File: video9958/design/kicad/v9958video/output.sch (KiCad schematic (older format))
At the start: 28 parts, among them J2 Conn_02x06_Counter_Clockwise, J3 DIN-6, Q2 2N3904, Q3 2N3906, Q4 2N3906, Q5 2N3906

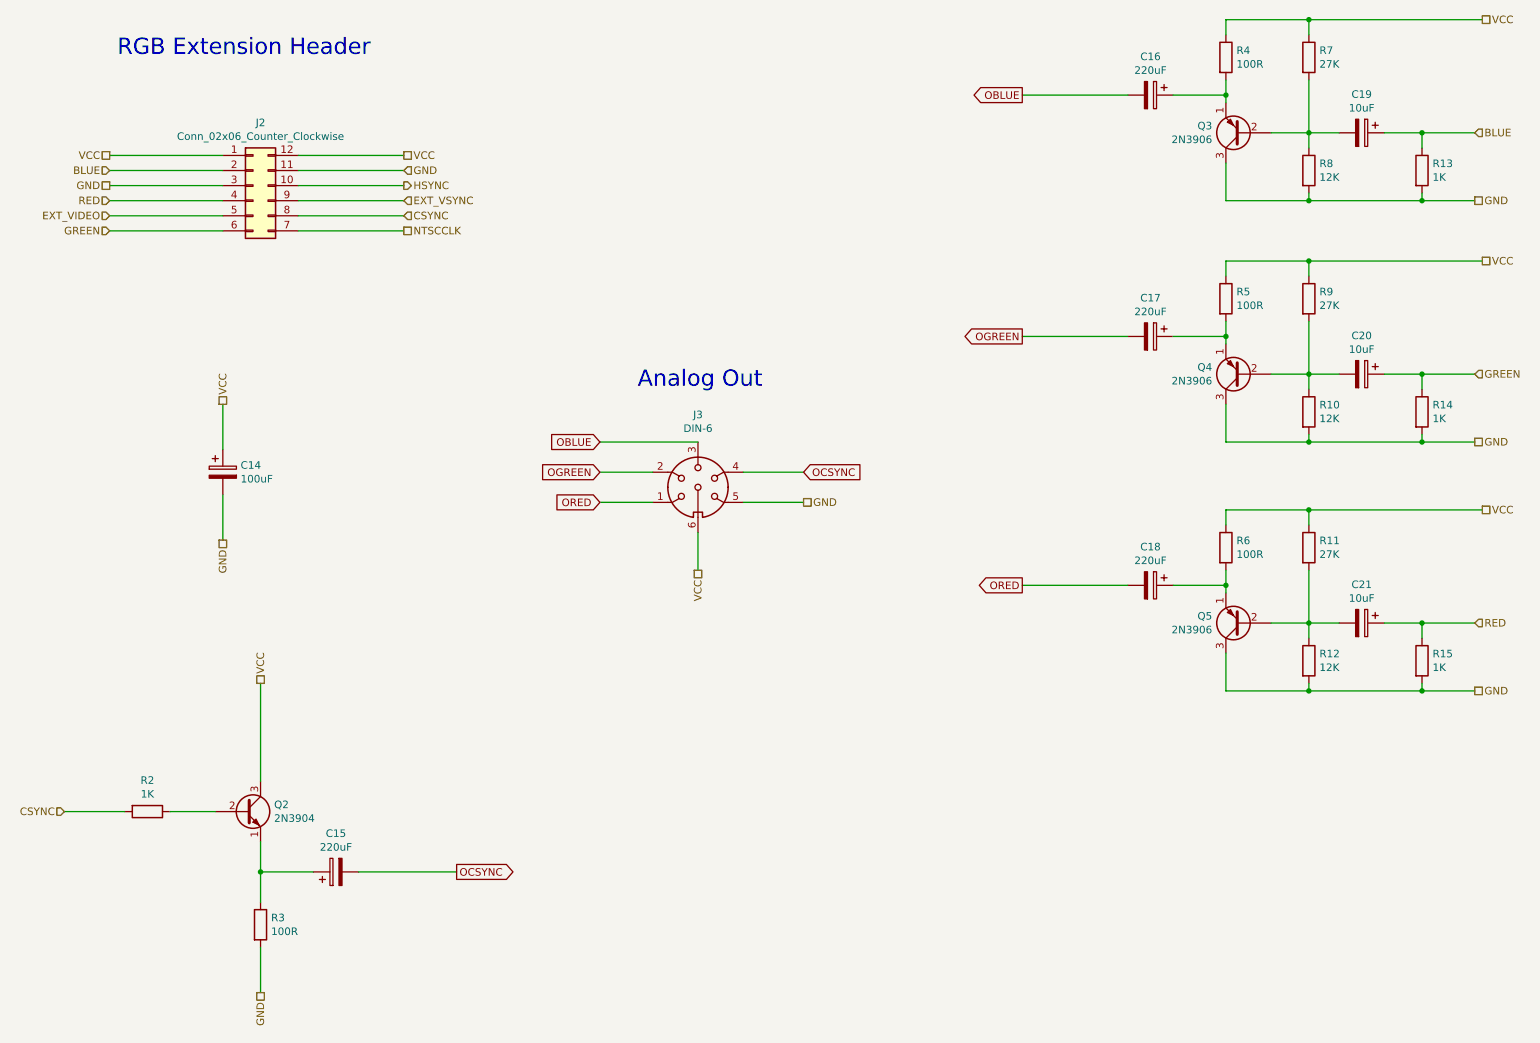
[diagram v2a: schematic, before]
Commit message: Rev 1 - Four layer board
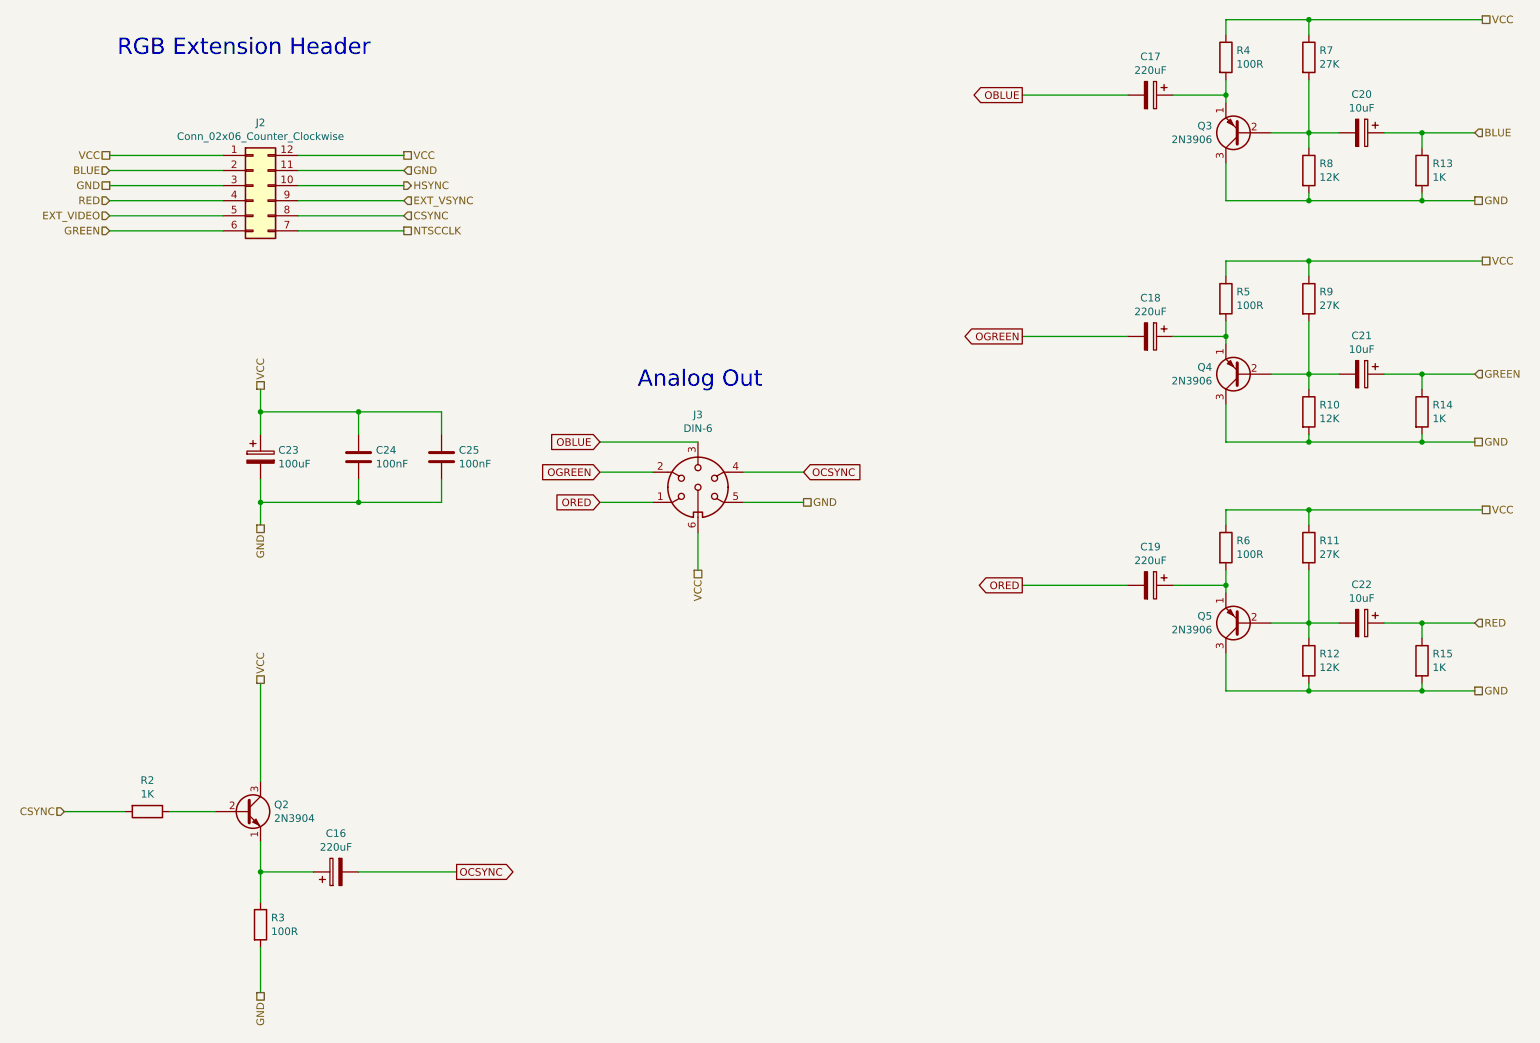
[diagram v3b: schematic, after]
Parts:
- added C24, C25: 100nF, Capacitor_THT:C_Rect_L7.0mm_W2.5mm_P5.00mm, symbol Device:C
- renumbered C15 to C16, C16 to C17, C17 to C18, C18 to C19, C19 to C20, C20 to C21, C21 to C22, C14 to C23
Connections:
- net GND: now also C24.2, C25.2
- net VCC: now also C24.1, C25.1
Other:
- moved on the sheet: C23
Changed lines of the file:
@@
 	2800 6450 2450 6450
 $Comp
-L Device:CP C15
+L Device:CP C16
 U 1 1 5EB8D33A
 P 2950 6450
-F 0 "C15" V 3205 6450 50  0000 C CNN
+F 0 "C16" V 3205 6450 50  0000 C CNN
 F 1 "220uF" V 3114 6450 50  0000 C CNN
 F 2 "Capacitor_THT:CP_Radial_D6.3mm_P2.50mm" H 2988 6300 50  0001 C CNN
@@
 $EndComp
 $Comp
-L Device:CP C21
+L Device:CP C22
 U 1 1 5EB704B0
 P 9750 4800
-F 0 "C21" V 9495 4800 50  0000 C CNN
+F 0 "C22" V 9495 4800 50  0000 C CNN
 F 1 "10uF" V 9586 4800 50  0000 C CNN
 F 2 "Capacitor_THT:CP_Radial_D5.0mm_P2.50mm" H 9788 4650 50  0001 C CNN
@@
 	8850 2800 8850 2900
 $Comp
-L Device:CP C17
+L Device:CP C18
 U 1 1 5EB5A4E3
 P 8350 2900
-F 0 "C17" V 8095 2900 50  0000 C CNN
+F 0 "C18" V 8095 2900 50  0000 C CNN
 F 1 "220uF" V 8186 2900 50  0000 C CNN
 F 2 "Capacitor_THT:CP_Radial_D6.3mm_P2.50mm" H 8388 2750 50  0001 C CNN
@@
 $EndComp
 $Comp
-L Device:CP C20
+L Device:CP C21
 U 1 1 5EB5A4AC
 P 9750 3150
-F 0 "C20" V 9495 3150 50  0000 C CNN
+F 0 "C21" V 9495 3150 50  0000 C CNN
 F 1 "10uF" V 9586 3150 50  0000 C CNN
 F 2 "Capacitor_THT:CP_Radial_D5.0mm_P2.50mm" H 9788 3000 50  0001 C CNN
@@
 	8850 1200 8850 1300
 $Comp
-L Device:CP C16
+L Device:CP C17
 U 1 1 5EB51CD3
 P 8350 1300
-F 0 "C16" V 8095 1300 50  0000 C CNN
+F 0 "C17" V 8095 1300 50  0000 C CNN
 F 1 "220uF" V 8186 1300 50  0000 C CNN
 F 2 "Capacitor_THT:CP_Radial_D6.3mm_P2.50mm" H 8388 1150 50  0001 C CNN
@@
 $EndComp
 $Comp
-L Device:CP C19
+L Device:CP C20
 U 1 1 5EB4735D
 P 9750 1550
-F 0 "C19" V 9495 1550 50  0000 C CNN
+F 0 "C20" V 9495 1550 50  0000 C CNN
 F 1 "10uF" V 9586 1550 50  0000 C CNN
 F 2 "Capacitor_THT:CP_Radial_D5.0mm_P2.50mm" H 9788 1400 50  0001 C CNN
@@
 	2700 1700 3400 1700
 $Comp
-L Device:CP C14
+L Device:CP C23
 U 1 1 5ECAC019
-P 2200 3800
-F 0 "C14" H 2318 3846 50  0000 L CNN
-F 1 "100uF" H 2318 3755 50  0000 L CNN
-F 2 "Capacitor_THT:CP_Radial_D5.0mm_P2.50mm" H 2238 3650 50  0001 C CNN
-F 3 "~" H 2200 3800 50  0001 C CNN
-	1    2200 3800
-	1    0    0    -1
-$EndComp
-Wire Wire Line
-	2200 3350 2200 3650
-Wire Wire Line
-	2200 3950 2200 4250
-Text HLabel 2200 3350 1    50   UnSpc ~ 0
-VCC
-Text HLabel 2200 4250 3    50   UnSpc ~ 0
-GND
-$Comp
-L Device:CP C18
+P 2450 3700
+F 0 "C23" H 2568 3746 50  0000 L CNN
+F 1 "100uF" H 2568 3655 50  0000 L CNN
+F 2 "Capacitor_THT:CP_Radial_D5.0mm_P2.50mm" H 2488 3550 50  0001 C CNN
+F 3 "~" H 2450 3700 50  0001 C CNN
+	1    2450 3700
+	1    0    0    -1
+$EndComp
+Wire Wire Line
+	2450 3250 2450 3400
+Wire Wire Line
+	2450 3850 2450 4000
+Text HLabel 2450 3250 1    50   UnSpc ~ 0
+VCC
+Text HLabel 2450 4150 3    50   UnSpc ~ 0
+GND
+$Comp
+L Device:CP C19
 U 1 1 5EB704E7
 P 8350 4550
-F 0 "C18" V 8095 4550 50  0000 C CNN
+F 0 "C19" V 8095 4550 50  0000 C CNN
 F 1 "220uF" V 8186 4550 50  0000 C CNN
 F 2 "Capacitor_THT:CP_Radial_D6.3mm_P2.50mm" H 8388 4400 50  0001 C CNN
@@
 	0    1    1    0
 $EndComp
+$Comp
+L Device:C C24
+U 1 1 5ECC1F41
+P 3100 3700
+F 0 "C24" H 3215 3746 50  0000 L CNN
+F 1 "100nF" H 3215 3655 50  0000 L CNN
+F 2 "Capacitor_THT:C_Rect_L7.0mm_W2.5mm_P5.00mm" H 3138 3550 50  0001 C CNN
+F 3 "~" H 3100 3700 50  0001 C CNN
+	1    3100 3700
+	1    0    0    -1
+$EndComp
+$Comp
+L Device:C C25
+U 1 1 5ECC26DA
+P 3650 3700
+F 0 "C25" H 3765 3746 50  0000 L CNN
+F 1 "100nF" H 3765 3655 50  0000 L CNN
+F 2 "Capacitor_THT:C_Rect_L7.0mm_W2.5mm_P5.00mm" H 3688 3550 50  0001 C CNN
+F 3 "~" H 3650 3700 50  0001 C CNN
+	1    3650 3700
+	1    0    0    -1
+$EndComp
+Wire Wire Line
+	3100 3550 3100 3400
+Wire Wire Line
+	3100 3400 2450 3400
+Connection ~ 2450 3400
+Wire Wire Line
+	2450 3400 2450 3550
+Wire Wire Line
+	3100 3400 3650 3400
+Wire Wire Line
+	3650 3400 3650 3550
+Connection ~ 3100 3400
+Wire Wire Line
+	3650 3850 3650 4000
+Wire Wire Line
+	3650 4000 3100 4000
+Connection ~ 2450 4000
+Wire Wire Line
+	2450 4000 2450 4150
+Wire Wire Line
+	3100 3850 3100 4000
+Connection ~ 3100 4000
+Wire Wire Line
+	3100 4000 2450 4000
 $EndSCHEMATC

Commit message: Revision 1.1 RTM
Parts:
- added C26: 100nF, Capacitor_THT:C_Rect_L7.0mm_W2.5mm_P5.00mm, symbol Device:C
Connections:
- net GND: now also C26.2
- net VCC: now also C26.1
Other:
- moved on the sheet: C23, C24, C25
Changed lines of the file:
@@
 L Device:CP C23
 U 1 1 5ECAC019
-P 2450 3700
-F 0 "C23" H 2568 3746 50  0000 L CNN
-F 1 "100uF" H 2568 3655 50  0000 L CNN
-F 2 "Capacitor_THT:CP_Radial_D5.0mm_P2.50mm" H 2488 3550 50  0001 C CNN
-F 3 "~" H 2450 3700 50  0001 C CNN
-	1    2450 3700
+P 1600 3700
+F 0 "C23" H 1718 3746 50  0000 L CNN
+F 1 "100uF" H 1718 3655 50  0000 L CNN
+F 2 "Capacitor_THT:CP_Radial_D5.0mm_P2.50mm" H 1638 3550 50  0001 C CNN
+F 3 "~" H 1600 3700 50  0001 C CNN
+	1    1600 3700
 	1    0    0    -1
 $EndComp
 Wire Wire Line
-	2450 3250 2450 3400
+	1600 3250 1600 3400
 Wire Wire Line
-	2450 3850 2450 4000
-Text HLabel 2450 3250 1    50   UnSpc ~ 0
+	1600 3850 1600 4000
+Text HLabel 1600 3250 1    50   UnSpc ~ 0
 VCC
-Text HLabel 2450 4150 3    50   UnSpc ~ 0
+Text HLabel 1600 4150 3    50   UnSpc ~ 0
 GND
 $Comp
@@
 L Device:C C24
 U 1 1 5ECC1F41
-P 3100 3700
-F 0 "C24" H 3215 3746 50  0000 L CNN
-F 1 "100nF" H 3215 3655 50  0000 L CNN
-F 2 "Capacitor_THT:C_Rect_L7.0mm_W2.5mm_P5.00mm" H 3138 3550 50  0001 C CNN
-F 3 "~" H 3100 3700 50  0001 C CNN
-	1    3100 3700
+P 2250 3700
+F 0 "C24" H 2365 3746 50  0000 L CNN
+F 1 "100nF" H 2365 3655 50  0000 L CNN
+F 2 "Capacitor_THT:C_Rect_L7.0mm_W2.5mm_P5.00mm" H 2288 3550 50  0001 C CNN
+F 3 "~" H 2250 3700 50  0001 C CNN
+	1    2250 3700
 	1    0    0    -1
 $EndComp
@@
 L Device:C C25
 U 1 1 5ECC26DA
-P 3650 3700
-F 0 "C25" H 3765 3746 50  0000 L CNN
-F 1 "100nF" H 3765 3655 50  0000 L CNN
-F 2 "Capacitor_THT:C_Rect_L7.0mm_W2.5mm_P5.00mm" H 3688 3550 50  0001 C CNN
-F 3 "~" H 3650 3700 50  0001 C CNN
-	1    3650 3700
+P 2800 3700
+F 0 "C25" H 2915 3746 50  0000 L CNN
+F 1 "100nF" H 2915 3655 50  0000 L CNN
+F 2 "Capacitor_THT:C_Rect_L7.0mm_W2.5mm_P5.00mm" H 2838 3550 50  0001 C CNN
+F 3 "~" H 2800 3700 50  0001 C CNN
+	1    2800 3700
 	1    0    0    -1
 $EndComp
 Wire Wire Line
-	3100 3550 3100 3400
+	2250 3550 2250 3400
 Wire Wire Line
-	3100 3400 2450 3400
-Connection ~ 2450 3400
+	2250 3400 1600 3400
+Connection ~ 1600 3400
 Wire Wire Line
-	2450 3400 2450 3550
+	1600 3400 1600 3550
 Wire Wire Line
-	3100 3400 3650 3400
+	2250 3400 2800 3400
 Wire Wire Line
-	3650 3400 3650 3550
-Connection ~ 3100 3400
+	2800 3400 2800 3550
+Connection ~ 2250 3400
 Wire Wire Line
-	3650 3850 3650 4000
+	2800 3850 2800 4000
 Wire Wire Line
-	3650 4000 3100 4000
-Connection ~ 2450 4000
+	2800 4000 2250 4000
+Connection ~ 1600 4000
 Wire Wire Line
-	2450 4000 2450 4150
+	1600 4000 1600 4150
 Wire Wire Line
-	3100 3850 3100 4000
-Connection ~ 3100 4000
+	2250 3850 2250 4000
+Connection ~ 2250 4000
 Wire Wire Line
-	3100 4000 2450 4000
+	2250 4000 1600 4000
+$Comp
+L Device:C C26
+U 1 1 5EDEB0AA
+P 3350 3700
+F 0 "C26" H 3465 3746 50  0000 L CNN
+F 1 "100nF" H 3465 3655 50  0000 L CNN
+F 2 "Capacitor_THT:C_Rect_L7.0mm_W2.5mm_P5.00mm" H 3388 3550 50  0001 C CNN
+F 3 "~" H 3350 3700 50  0001 C CNN
+	1    3350 3700
+	1    0    0    -1
+$EndComp
+Wire Wire Line
+	2800 3400 3350 3400
+Wire Wire Line
+	3350 3400 3350 3550
+Connection ~ 2800 3400
+Wire Wire Line
+	2800 4000 3350 4000
+Wire Wire Line
+	3350 4000 3350 3850
+Connection ~ 2800 4000
 $EndSCHEMATC
